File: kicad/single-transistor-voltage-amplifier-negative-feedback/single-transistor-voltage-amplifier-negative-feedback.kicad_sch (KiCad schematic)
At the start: 13 parts, among them J1 NMJ4HHD2, J2 NMJ4HHD2, J3 Screw_Terminal_01x02, Q1 BC337

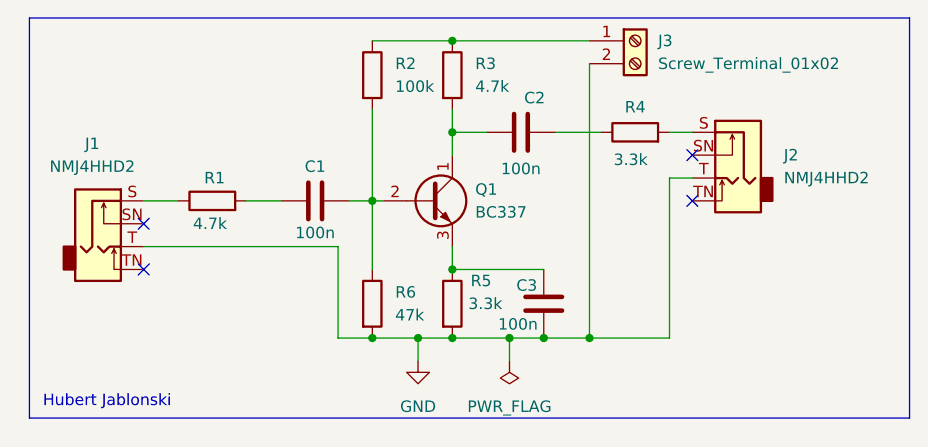
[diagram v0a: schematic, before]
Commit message: Add single-transistor-voltage-amplifier-negative-feedback and update readme
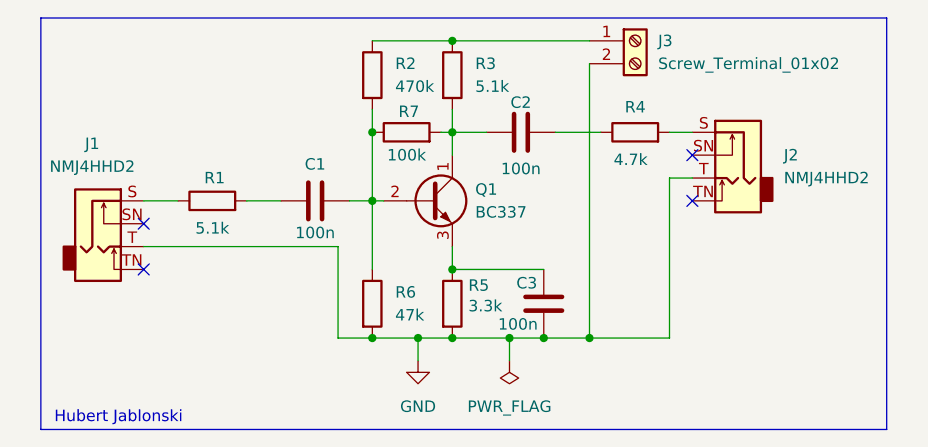
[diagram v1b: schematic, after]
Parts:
- added R7: 100k, Resistor_THT:R_Axial_DIN0204_L3.6mm_D1.6mm_P1.90mm_Vertical, symbol Device:R
- R1, R3: value 4.7k -> 5.1k
- R2: value 100k -> 470k
- R4: value 3.3k -> 4.7k
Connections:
- net at C1.2, Q1.2 (B), R2.2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: now also R7.1
- net at C2.1, Q1.1 (C), R3.2: now also R7.2
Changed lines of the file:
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@@
 	(paper "A4")
 	(rectangle
-		(start 76.2 60.96)
-		(end 173.99 105.41)
+		(start 77.47 60.96)
+		(end 171.45 106.68)
 		(stroke
 			(width 0)
@@
 	(text "Hubert Jablonski"
 		(exclude_from_sim no)
-		(at 84.836 103.632 0)
+		(at 86.106 105.41 0)
 		(effects
 			(font
@@
 	)
 	(junction
+		(at 114.3 73.66)
+		(diameter 0)
+		(color 0 0 0 0)
+	)
+	(junction
 		(at 133.35 96.52)
 		(diameter 0)
@@
 	(wire
 		(pts
+			(xy 114.3 73.66) (xy 114.3 81.28)
+		)
+		(stroke
+			(width 0)
+			(type default)
+		)
+	)
+	(wire
+		(pts
 			(xy 123.19 73.66) (xy 123.19 76.2)
 		)
@@
 	(wire
 		(pts
+			(xy 121.92 73.66) (xy 123.19 73.66)
+		)
+		(stroke
+			(width 0)
+			(type default)
+		)
+	)
+	(wire
+		(pts
 			(xy 129.54 96.52) (xy 133.35 96.52)
 		)
@@
 	(wire
 		(pts
-			(xy 114.3 71.12) (xy 114.3 81.28)
+			(xy 114.3 71.12) (xy 114.3 73.66)
 		)
 		(stroke
@@
 			)
 		)
-		(property "Value" "4.7k"
-			(at 96.266 83.82 90)
+		(property "Value" "5.1k"
+			(at 96.52 84.328 90)
 			(effects
 				(font
@@
 		(dnp no)
 		(property "Reference" "C3"
-			(at 130.302 90.678 0)
+			(at 130.302 90.424 0)
 			(effects
 				(font
@@
 			)
 		)
-		(property "Value" "3.3k"
+		(property "Value" "4.7k"
 			(at 143.002 76.708 90)
 			(effects
@@
 			)
 		)
-		(property "Value" "100k"
+		(property "Value" "470k"
 			(at 116.84 68.5799 0)
 			(effects
@@
 		(dnp no)
 		(property "Reference" "C1"
-			(at 107.95 77.47 90)
+			(at 107.95 77.216 90)
 			(effects
 				(font
@@
 			)
 		)
-		(property "Value" "4.7k"
+		(property "Value" "5.1k"
 			(at 125.73 68.5799 0)
 			(effects
@@
 		(dnp no)
 		(property "Reference" "C2"
-			(at 132.334 69.85 90)
+			(at 130.81 70.358 90)
 			(effects
 				(font
@@
 		(dnp no)
 		(property "Reference" "R5"
-			(at 125.222 90.17 0)
+			(at 124.968 90.678 0)
 			(effects
 				(font
@@
 		)
 		(property "Value" "3.3k"
-			(at 124.968 92.71 0)
+			(at 124.968 92.964 0)
 			(effects
 				(font
@@
 					(unit 1)
 				)
+			)
+		)
+	)
+	(symbol
+		(lib_id "Device:R")
+		(at 118.11 73.66 90)
+		(unit 1)
+		(exclude_from_sim no)
+		(in_bom yes)
+		(on_board yes)
+		(dnp no)
+		(property "Reference" "R7"
+			(at 118.364 71.374 90)
+			(effects
+				(font
+					(size 1.27 1.27)
+				)
+			)
+		)
+		(property "Value" "100k"
+			(at 118.11 76.2 90)
+			(effects
+				(font
+					(size 1.27 1.27)
+				)
+			)
+		)
+		(property "Footprint" "Resistor_THT:R_Axial_DIN0204_L3.6mm_D1.6mm_P1.90mm_Vertical"
+			(at 118.11 75.438 90)
+			(effects
+				(font
+					(size 1.27 1.27)
+				)
+				(hide yes)
+			)
+		)
+		(property "Datasheet" "~"
+			(at 118.11 73.66 0)
+			(effects
+				(font
+					(size 1.27 1.27)
+				)
+				(hide yes)
+			)
+		)
+		(property "Description" "Resistor"
+			(at 118.11 73.66 0)
+			(effects
+				(font
+					(size 1.27 1.27)
+				)
+				(hide yes)
+			)
+		)
+		(pin "2"
+		)
+		(pin "1"
+		)
+		(instances
+			(project ""
+				(path "/5e41f121-57a3-4db6-a68b-c38648245487"
+					(reference "R7")
+					(unit 1)
+				)
